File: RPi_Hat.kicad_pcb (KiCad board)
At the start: 2 copper layers, 65 x 56 mm, 50 parts, among them J1 Conn_01x02_Male, J2 RPi_GPIO, J3 Conn_02x03_Counter_Clockwise, J5 Conn_01x03_Male, J6 Conn_01x03_Male, J7 Conn_01x03_Male, J8 Conn_01x03_Male, J9 Conn_01x03_Male, SW1 SW_Push, U1 LM1085-5.0, U2 STM32F030CCTx, U3 MAX485E, U4 MAX485E, U5 MAX485E, U6 MAX485E, U7 MAX485E

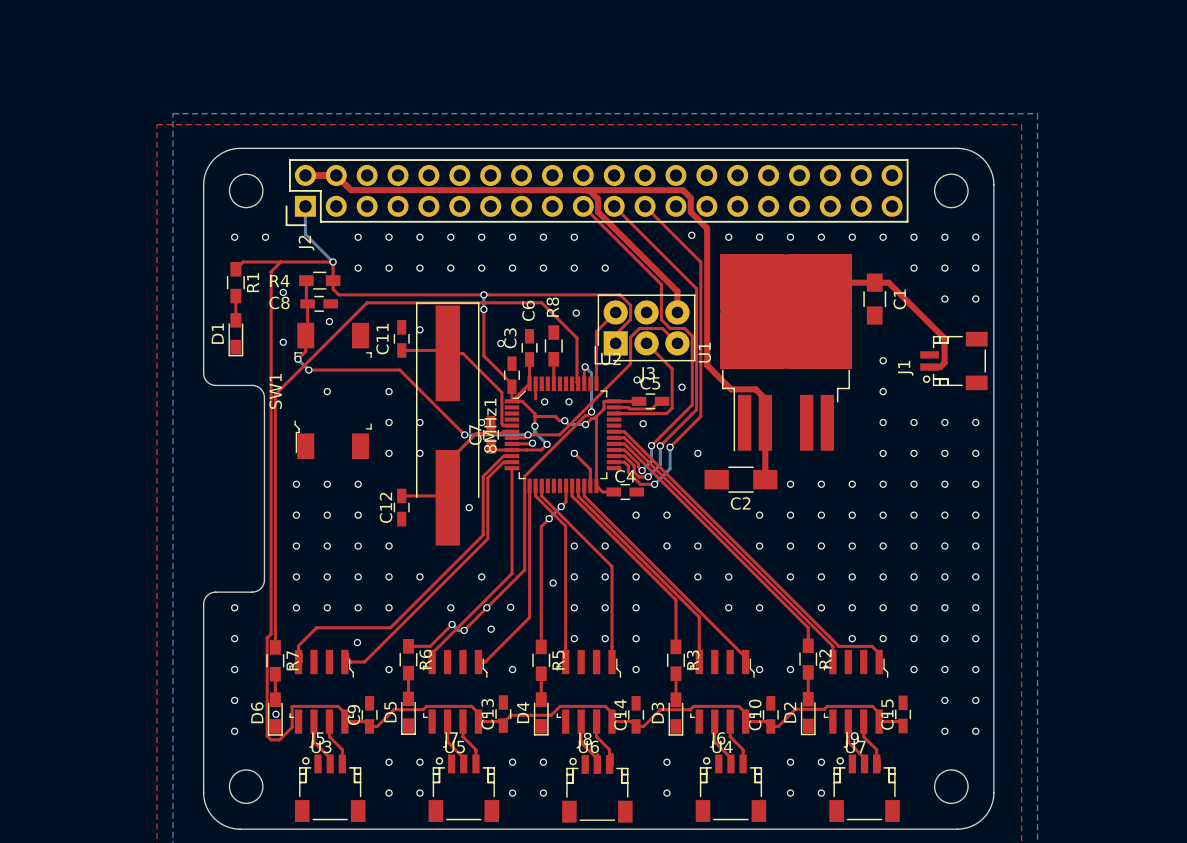
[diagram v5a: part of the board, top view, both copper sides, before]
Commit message: Add silkscreen info
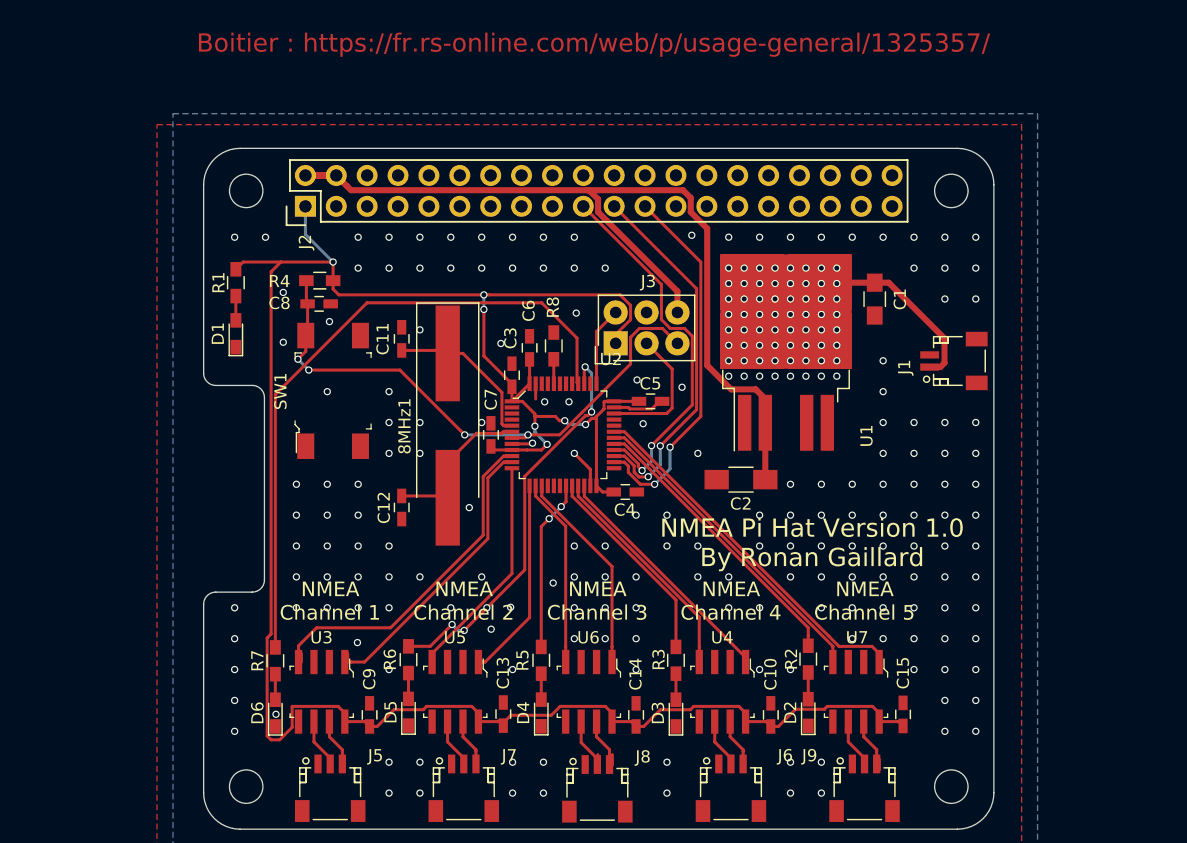
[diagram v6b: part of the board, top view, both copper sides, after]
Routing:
- net Net-(C1-Pad1): track 19.3 -> 15.6 mm, vias 0 -> 56
- net Net-(J5-Pad2): vias 0 -> 1
- net GND: vias 183 -> 190
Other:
- board text added: "Boitier : https://fr.rs-online.com/web/p/usage-general/1325357/"
- board text added: "NMEA Channel 1"
- board text added: "NMEA Channel 2"
- board text added: "NMEA Channel 3"
- board text added: "NMEA Channel 4"
- board text added: "NMEA Channel 5"
- board text added: "NMEA Pi Hat Version 1.0 By Ronan Gaillard"

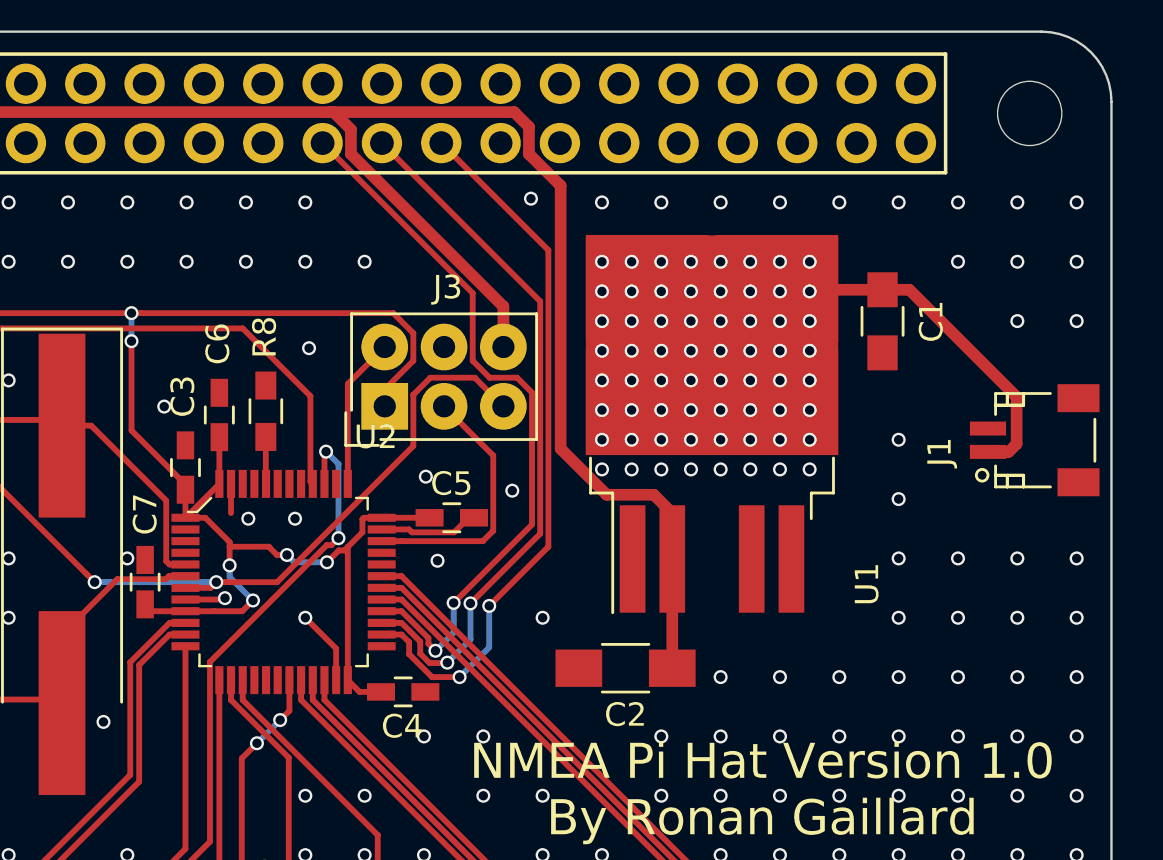
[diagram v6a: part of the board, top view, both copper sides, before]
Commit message: Connect reset and boot0 to raspi and change few things
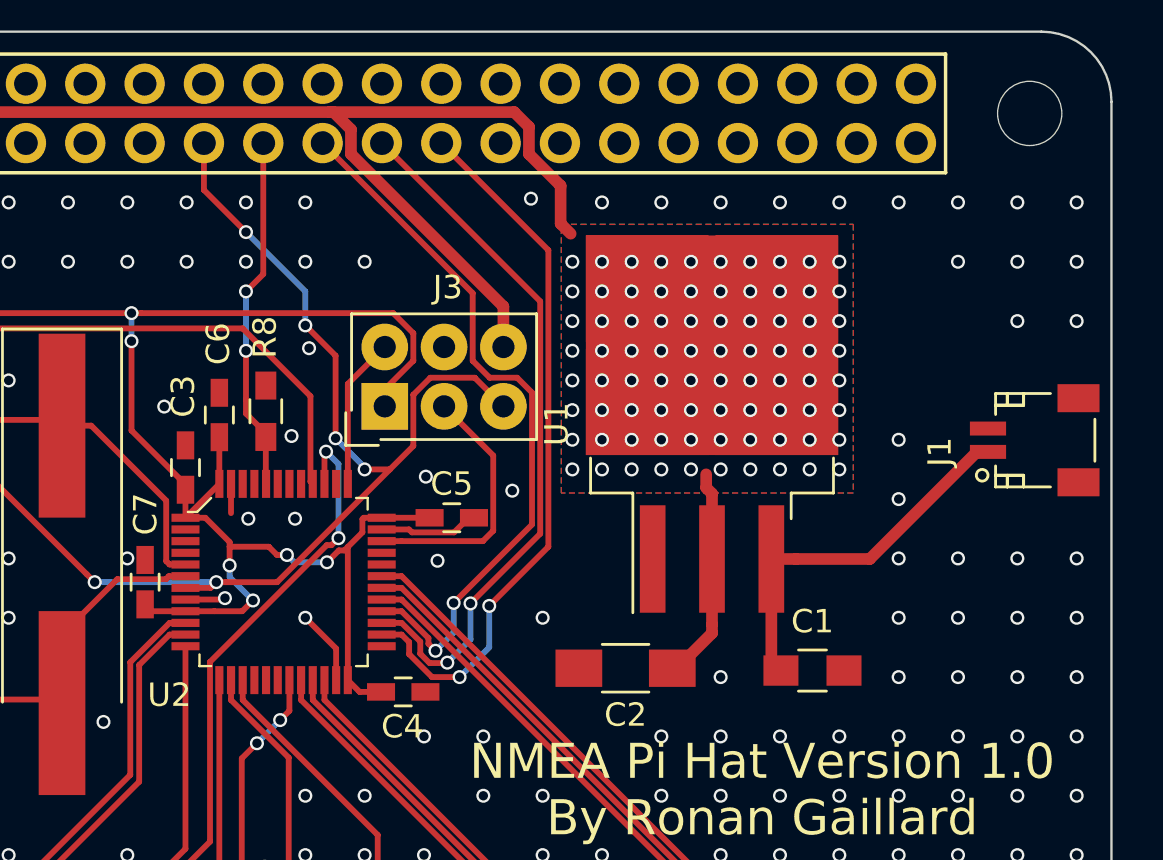
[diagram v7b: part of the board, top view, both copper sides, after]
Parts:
- U1: footprint TO_SOT_Packages_SMD:TO-263-4 -> TO_SOT_Packages_SMD:TO-263-3_TabPin2
- moved C1 15.2 mm to (87.8, 55.6), turned to 0 degrees
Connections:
- J2 pad 15: Net-(J2-Pad15) -> /RPi_GPIO/RESET
- J2 pad 17: Net-(J2-Pad17) -> /RPi_GPIO/BOOT0
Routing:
- net /RPi_GPIO/RESET: track 47.8 -> 65.7 mm, vias 4 -> 8
- net /RPi_GPIO/BOOT0: track 2.01 -> 15.3 mm, vias 0 -> 2
- net +5V: track 75.4 -> 65.0 mm, vias 0 -> 80
- net Net-(C1-Pad1): track 15.6 -> 16.1 mm, vias 56 -> 0
- net Net-(J5-Pad2): vias 1 -> 0
- net GND: vias 190 -> 182
- added copper zone on B.Cu, net +5V
- added copper zone on F.Cu, net +5V

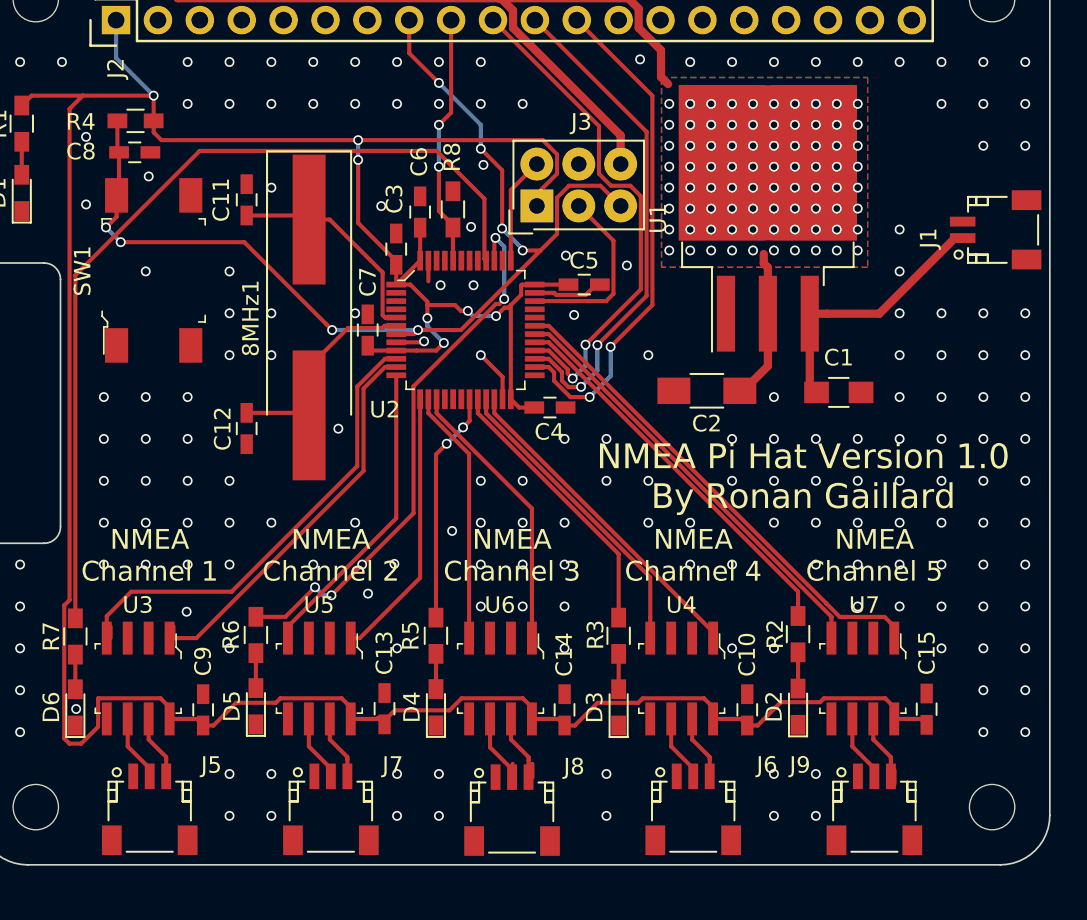
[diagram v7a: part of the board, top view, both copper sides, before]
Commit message: Add some vias
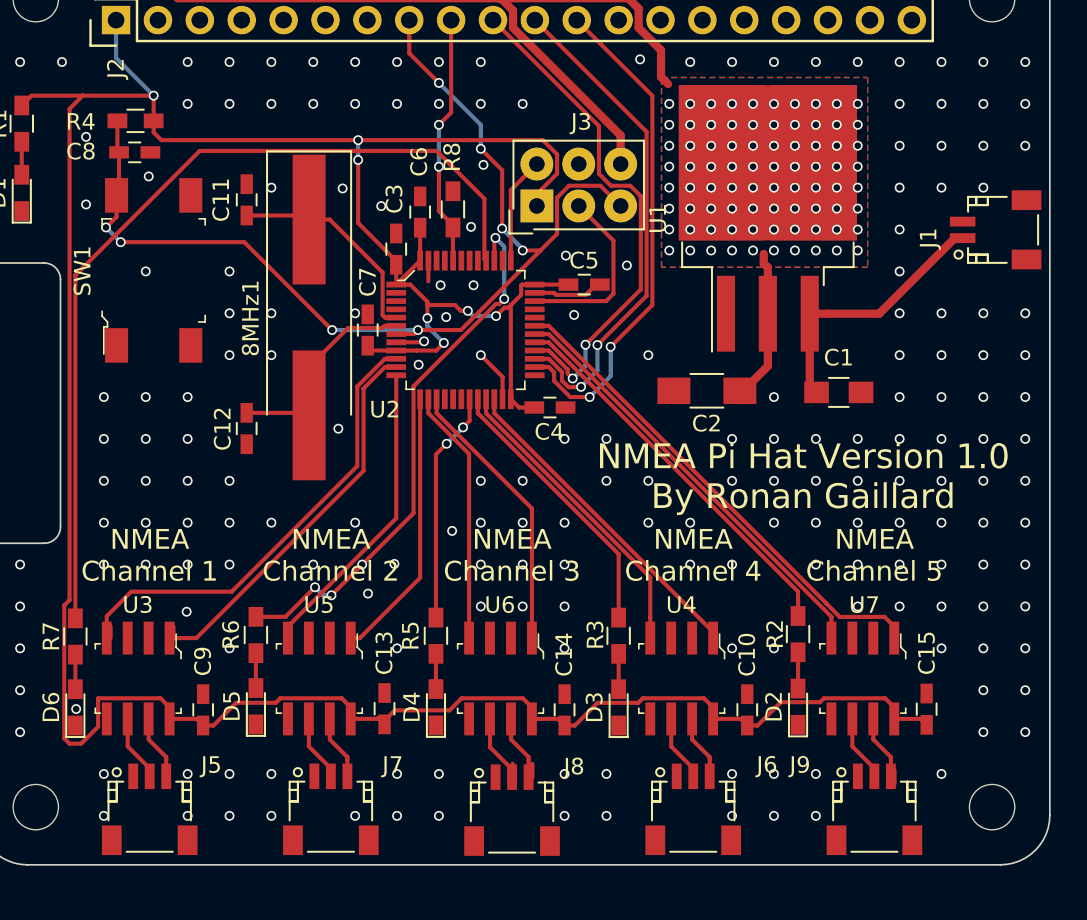
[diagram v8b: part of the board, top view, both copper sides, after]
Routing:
- net GND: vias 182 -> 201
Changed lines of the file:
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@@
     (thickness 1.6)
     (drawings 37)
-    (tracks 665)
+    (tracks 684)
     (zones 0)
     (modules 50)
@@
   (via (at 78.74 35.56) (size 0.6) (drill 0.4) (layers F.Cu B.Cu) (net 25))
   (via (at 65.45 45.56) (size 0.6) (drill 0.4) (layers F.Cu B.Cu) (net 25))
+  (via (at 57.66 43.23) (size 0.6) (drill 0.4) (layers F.Cu B.Cu) (net 25))
+  (via (at 62.27 53.92) (size 0.6) (drill 0.4) (layers F.Cu B.Cu) (net 25))
+  (via (at 63.94 51.03) (size 0.6) (drill 0.4) (layers F.Cu B.Cu) (net 25))
+  (via (at 93.98 40.64) (size 0.6) (drill 0.4) (layers F.Cu B.Cu) (net 25))
+  (via (at 91.44 38.1) (size 0.6) (drill 0.4) (layers F.Cu B.Cu) (net 25))
+  (via (at 91.44 40.64) (size 0.6) (drill 0.4) (layers F.Cu B.Cu) (net 25))
+  (via (at 91.44 43.18) (size 0.6) (drill 0.4) (layers F.Cu B.Cu) (net 25))
+  (via (at 93.98 43.18) (size 0.6) (drill 0.4) (layers F.Cu B.Cu) (net 25))
+  (via (at 96.52 43.18) (size 0.6) (drill 0.4) (layers F.Cu B.Cu) (net 25))
+  (via (at 71.12 78.74) (size 0.6) (drill 0.4) (layers F.Cu B.Cu) (net 25))
+  (via (at 71.12 81.28) (size 0.6) (drill 0.4) (layers F.Cu B.Cu) (net 25))
+  (via (at 81.28 78.74) (size 0.6) (drill 0.4) (layers F.Cu B.Cu) (net 25))
+  (via (at 81.28 81.28) (size 0.6) (drill 0.4) (layers F.Cu B.Cu) (net 25))
+  (via (at 93.98 78.74) (size 0.6) (drill 0.4) (layers F.Cu B.Cu) (net 25))
+  (via (at 58.42 81.28) (size 0.6) (drill 0.4) (layers F.Cu B.Cu) (net 25))
+  (via (at 48.26 81.28) (size 0.6) (drill 0.4) (layers F.Cu B.Cu) (net 25))
+  (via (at 48.26 78.74) (size 0.6) (drill 0.4) (layers F.Cu B.Cu) (net 25))
+  (via (at 43.18 78.74) (size 0.6) (drill 0.4) (layers F.Cu B.Cu) (net 25))
+  (via (at 43.18 81.28) (size 0.6) (drill 0.4) (layers F.Cu B.Cu) (net 25))
   (segment (start 43.92 30.48) (end 46.46 30.48) (width 0.5) (layer F.Cu) (net 26))
   (segment (start 46.46 30.48) (end 43.922798 30.48) (width 0.5) (layer F.Cu) (net 26))
